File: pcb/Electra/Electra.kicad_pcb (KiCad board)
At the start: 2 copper layers, 100 x 48.5 mm, 77 parts, among them J101 Extra1, J102 RTC, J103 Extra2, J104 UART, J201 USB, J202 7-12V, J301 Relay 2/D, J401 S1/U, J402 S2/D, J601 A, J602 A2, J701 RF433, J801 Relay 1/U, K301 FINDER-36.11, K801 FINDER-36.11, Q301 Q_NPN_EBC, Q801 Q_NPN_EBC, SW501 Flash, SW502 RST, U201 AMS1117-5.0, U202 AMS1117-3.3, U501 ESP-12F

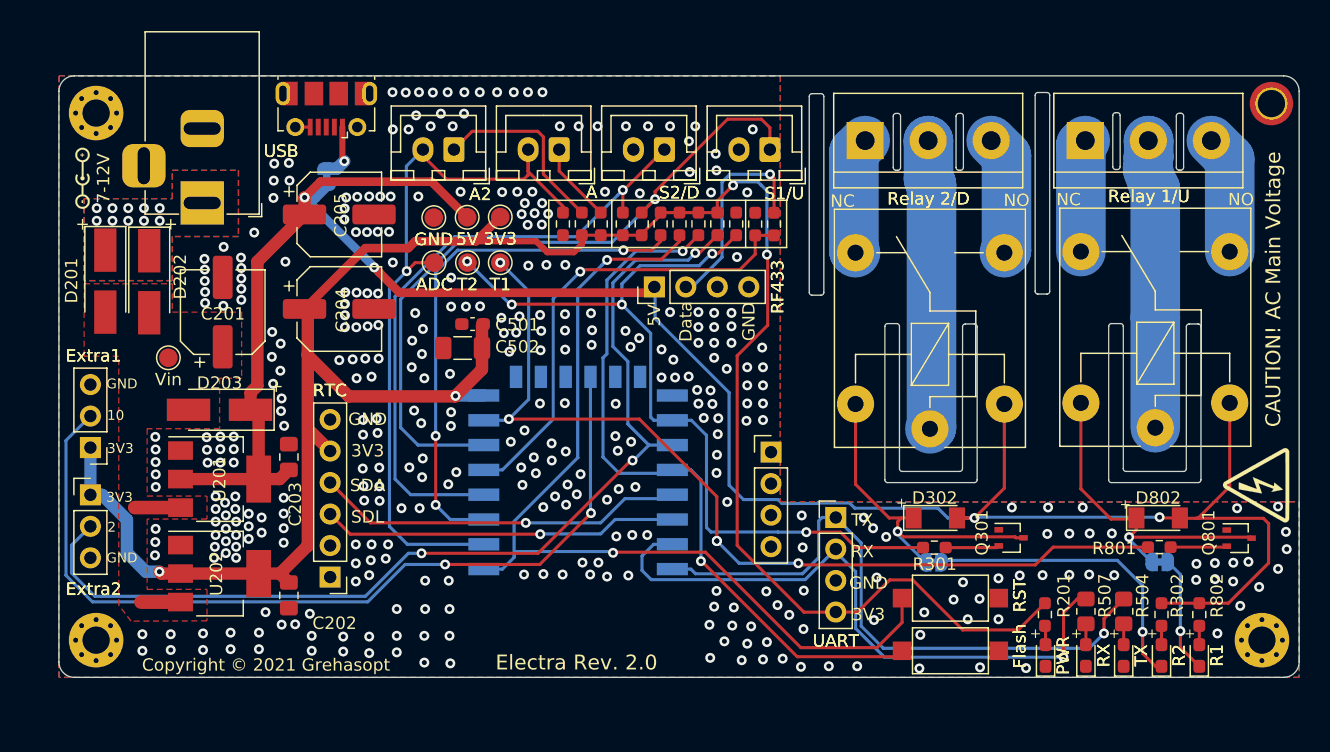
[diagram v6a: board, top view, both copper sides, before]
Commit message: Clean some vias and clean up files
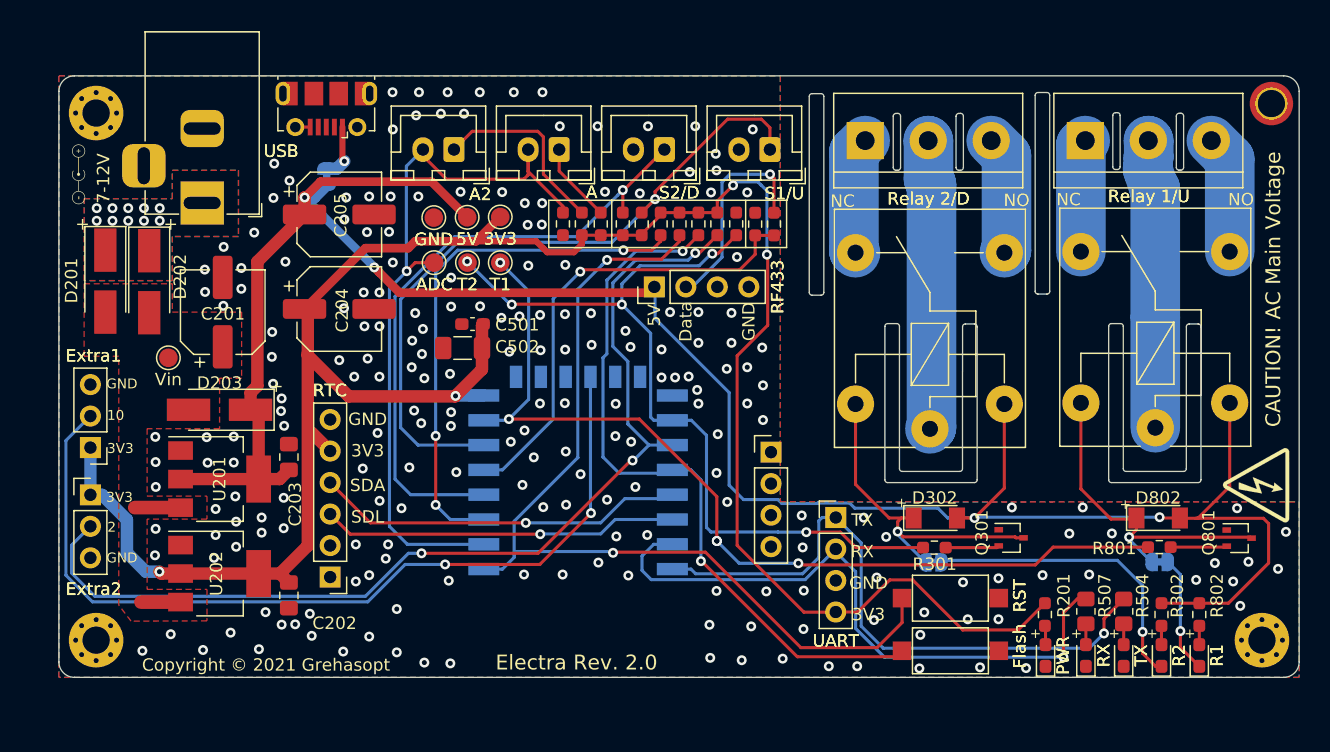
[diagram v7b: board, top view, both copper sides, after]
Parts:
- removed the G*** at (99.4, 78.8)
- added G***: LOGO, Custom:dc-barrel-positive-polarity-5.1x5, F.Cu at (99.1, 78.4)
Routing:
- net GND: vias 367 -> 216
- net (no net): vias 6 -> 2

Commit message: Minor fixes on schematic and pcb fix bjt netlist + ac main voltage to both sides (Rev 2.1)
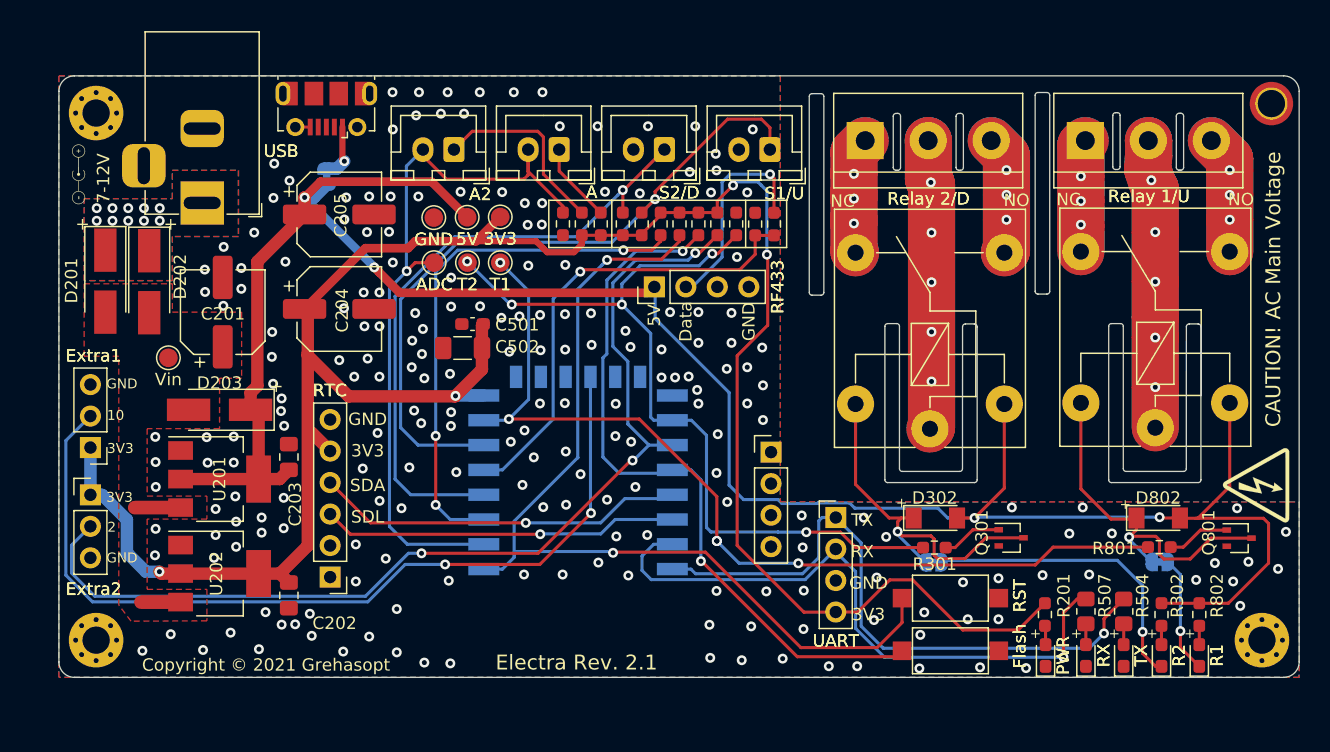
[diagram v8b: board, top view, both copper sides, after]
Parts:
- JP201: value USB-IN -> Jumper_NC_Small
- JP301: value R2 -> Jumper_NC_Small
- JP801: value R1 -> Jumper_NC_Small
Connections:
- Q301 pad 1: GND -> Net-(Q301-Pad1)
- Q301 pad 2: Net-(Q301-Pad2) -> GND
- Q801 pad 1: GND -> Net-(Q801-Pad1)
- Q801 pad 2: Net-(Q801-Pad2) -> GND
- R301 pad 1: Net-(Q301-Pad2) -> Net-(Q301-Pad1)
- R801 pad 1: Net-(Q801-Pad2) -> Net-(Q801-Pad1)
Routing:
- net /Relay2/Relay-Common: track 23.4 -> 46.8 mm, vias 0 -> 5
- net /Relay1/Relay-Common: track 23.3 -> 46.6 mm, vias 0 -> 5
- net /Relay2/Relay-Normal-Open: track 9.62 -> 19.2 mm, vias 0 -> 3
- net /Relay1/Relay-Normal-Open: track 9.56 -> 19.1 mm, vias 0 -> 3
- net /Relay2/Relay-Normal-Close: track 9.47 -> 18.9 mm, vias 0 -> 3
- net /Relay1/Relay-Normal-Close: track 9.09 -> 18.2 mm, vias 0 -> 3
- net Net-(Q801-Pad1): track 0.00 -> 5.10 mm
- net Net-(Q301-Pad1): track 0.00 -> 4.87 mm
- net Net-(Q801-Pad2): track 4.56 -> 0.00 mm
- net Net-(Q301-Pad2): track 4.33 -> 0.00 mm
- net Net-(D802-Pad1): track 27.1 -> 29.3 mm
- net Net-(D302-Pad1): track 27.3 -> 29.4 mm
- net GND: track 1.20 -> 1.30 mm, vias 216 -> 214
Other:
- board text added: "Electra Rev. 2.1"
- board text removed: "Electra Rev. 2.0"
